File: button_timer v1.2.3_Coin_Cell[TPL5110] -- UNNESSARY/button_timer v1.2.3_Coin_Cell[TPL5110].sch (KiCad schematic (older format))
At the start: 26 parts, among them J1 Conn_01x05_Female, Q1 TSM2323, Q2 TSM2323, SW1 SW_Push, SW2 SW_Push, U1 TPS61097A, U2 TPL5110, X1 ESP-12E

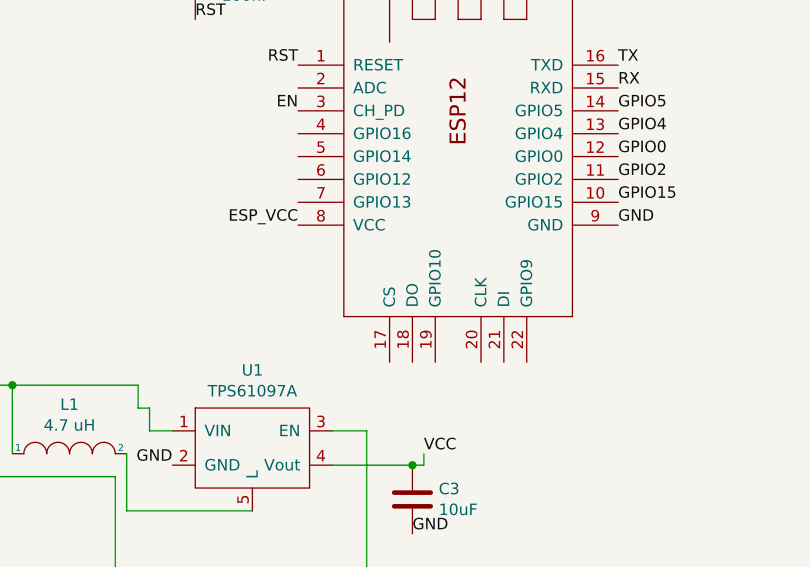
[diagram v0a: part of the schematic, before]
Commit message: cap added between vcc and gnd of the esp
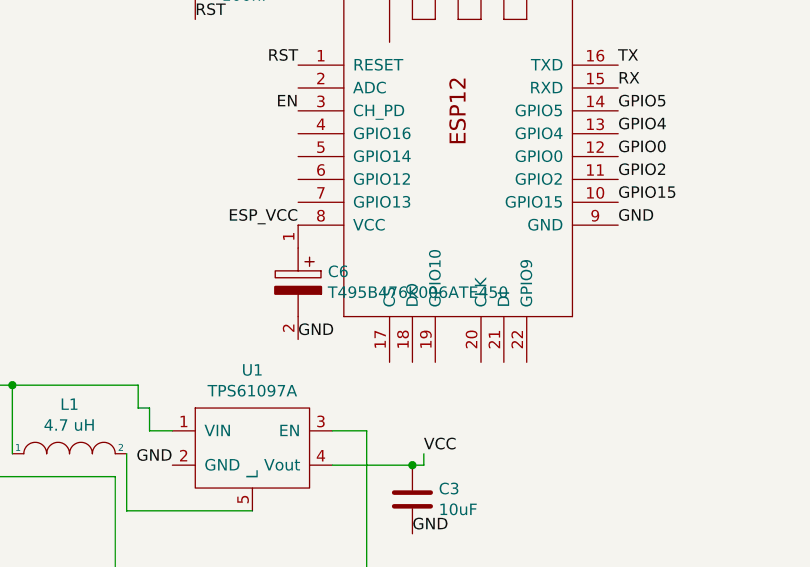
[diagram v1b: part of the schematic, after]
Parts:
- added C6: T495B476K006ATE450, CAPPM3528X210N, symbol SamacSys_Parts:T495B476K006ATE450
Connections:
- net ESP_VCC: now also C6.1
- net GND: now also C6.2
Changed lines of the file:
@@
 Text Label 4000 6250 2    50   ~ 0
 VCC
+$Comp
+L SamacSys_Parts:T495B476K006ATE450 C6
+U 1 1 60365DC7
+P 5300 3700
+F 0 "C6" V 5504 3830 50  0000 L CNN
+F 1 "T495B476K006ATE450" V 5595 3830 50  0000 L CNN
+F 2 "CAPPM3528X210N" H 5650 3750 50  0001 L CNN
+F 3 "https://connect.kemet.com:7667/gateway/IntelliData-ComponentDocumentation/1.0/download/specsheet/T495B476K006ATE450" H 5650 3650 50  0001 L CNN
+F 4 "Cap Tant Solid 47uF 6.3V B CASE 10% (3.5 X 2.8 X 1.9mm) SMD 3528-21 0.45 Ohm 125C Automotive T/R" H 5650 3550 50  0001 L CNN "Description"
+F 5 "2.1" H 5650 3450 50  0001 L CNN "Height"
+F 6 "Kemet" H 5650 3350 50  0001 L CNN "Manufacturer_Name"
+F 7 "T495B476K006ATE450" H 5650 3250 50  0001 L CNN "Manufacturer_Part_Number"
+F 8 "80-T495B476K6ATE450" H 5650 3150 50  0001 L CNN "Mouser Part Number"
+F 9 "https://www.mouser.com/Search/Refine.aspx?Keyword=80-T495B476K6ATE450" H 5650 3050 50  0001 L CNN "Mouser Price/Stock"
+F 10 "T495B476K006ATE450" H 5650 2950 50  0001 L CNN "Arrow Part Number"
+F 11 "https://www.arrow.com/en/products/t495b476k006ate450/kemet-corporation" H 5650 2850 50  0001 L CNN "Arrow Price/Stock"
+	1    5300 3700
+	0    1    1    0
+$EndComp
+Text Label 5300 4200 0    50   ~ 0
+GND
 $EndSCHEMATC
